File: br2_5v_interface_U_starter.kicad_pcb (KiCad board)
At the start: 4 copper layers, 94 x 76.2 mm, 18 parts, among them J10 BR2_BANK_A_J10, J11 BR2_BANK_B_J11, J12 BR2_BANK_B_J12, J13 BR2_BANK_B_J13, J14 BR2_BANK_B_J14, J17 BR2_CONTROL_J17, J18 BR2_CONTROL_J18, J19 BR2_CONTROL_J19, J20 BR2_CONTROL_J20, J21 5V_OUTPUTS_U1, J7 BR2_BANK_A_J7, J8 BR2_BANK_A_J8, J9 BR2_BANK_A_J9, U1 SN74AHCT245N

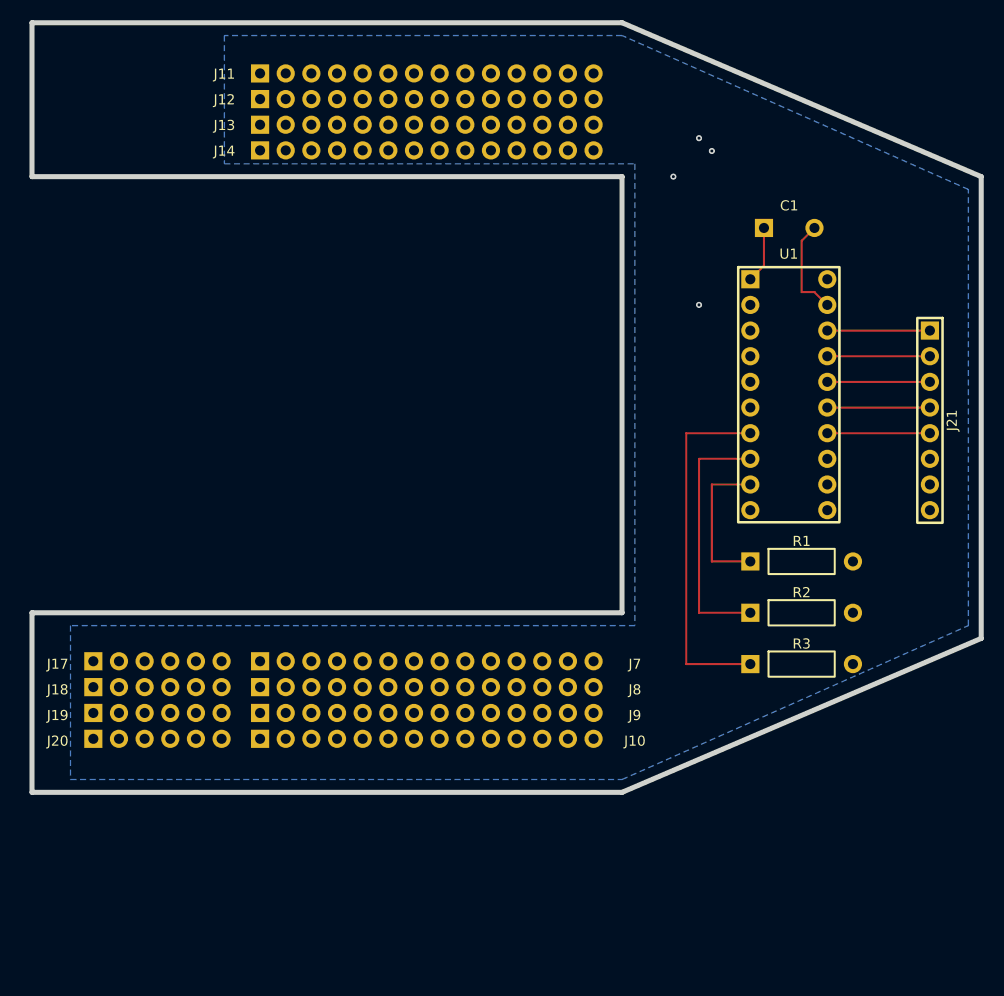
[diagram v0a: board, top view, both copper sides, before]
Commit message: Mac version: align BR2 headers and update PCB routing
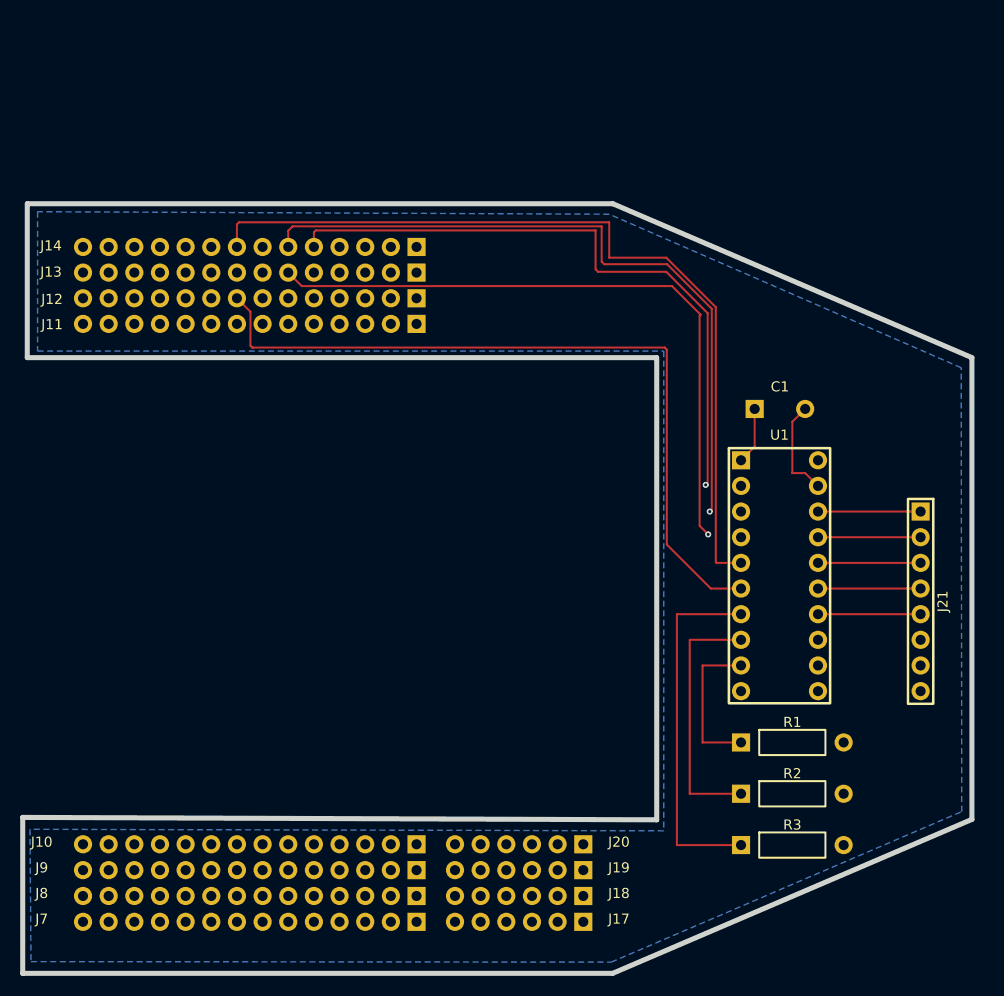
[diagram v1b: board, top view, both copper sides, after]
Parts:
- moved J17 54.9 mm to (148.6, 137.3), turned to 180 degrees
- moved J18 52.7 mm to (148.6, 134.7), turned to 180 degrees
- moved J19 50.9 mm to (148.6, 132.2), turned to 180 degrees
- moved J20 49.6 mm to (148.6, 129.6), turned to 180 degrees
- moved J7 30.1 mm to (132.1, 137.3), turned to 180 degrees
- moved J11 29.2 mm to (132.1, 78.1), turned to 180 degrees
- moved J8 25.8 mm to (132.1, 134.7), turned to 180 degrees
- moved J12 25.1 mm to (132.1, 75.5), turned to 180 degrees
- moved J9 22.0 mm to (132.1, 132.2), turned to 180 degrees
- moved J13 21.3 mm to (132.1, 73.0), turned to 180 degrees
- moved J10 18.7 mm to (132.1, 129.6), turned to 180 degrees
- moved J14 18.2 mm to (132.1, 70.5), turned to 180 degrees
- moved C1 17.9 mm to (165.5, 86.5)
- moved J21 17.9 mm to (182.0, 96.7)
- moved R1 17.9 mm to (164.2, 119.5)
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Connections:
- J20 pad 1: (no net) -> +5V
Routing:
- net +5V: track 13.3 -> 65.9 mm
- net B42_ROM_CS_N: track 57.0 -> 83.0 mm
- net B30_ACIA_CS_N: track 50.2 -> 72.5 mm
- net B41_HEARTBEAT_1KHZ: track 60.5 -> 75.4 mm, vias 1 -> 0
- net B24_RAM_CS_N: track 52.2 -> 67.0 mm, vias 0 -> 1
- net B28_UART_B_CS_N: track 57.2 -> 68.3 mm, vias 2 -> 1
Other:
- outline, holes or cut-outs redrawn

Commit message: Finalize Mac PCB for fabrication
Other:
- board text added: "6502 CS/"
- board text added: "BR2 5V INTERFACE REV 1.0 © 2026 Stanley Benoit"
- board text added: "FPGA CTRL Port"
- board text added: "FPGA Port A"
- board text added: "FPGA Port B"

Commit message: Correct 5V and 3.3V connections
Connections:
- J20 pad 1: +5V -> +3.3vdc
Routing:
- net +5V: track 65.9 -> 66.9 mm

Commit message: Update BR2 interface PCB and schematic with corrected pin mappings
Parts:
- C1: value 0.1uF -> 0.1uf
- J9: value BR2_BANK_A_J9 -> BR2_BANK _A_J9
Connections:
- net ACIA_CS_N_5V renamed /ACIA_CS_N_5V
- net B41_HEARTBEAT_1KHZ renamed /B41_HEARTBEAT_1KHZ
- net HEARTBEAT_1KHZ_5V renamed /HEARTBEAT_1KHZ_5V
- net RAM_CS_N_5V renamed /RAM_CS_N_5V
- net ROM_CS_N_5V renamed /ROM_CS_N_5V
- net UART_B_CS_N_5V renamed /UART_B_CS_N_5V
- J10 pad 1: (no net) -> unconnected-(J10-Pin_1-Pad1)
- J10 pad 10: (no net) -> unconnected-(J10-Pin_10-Pad10)
- J10 pad 11: (no net) -> unconnected-(J10-Pin_11-Pad11)
- J10 pad 12: (no net) -> unconnected-(J10-Pin_12-Pad12)
- J10 pad 13: (no net) -> unconnected-(J10-Pin_13-Pad13)
- J10 pad 14: (no net) -> unconnected-(J10-Pin_14-Pad14)
- J10 pad 2: (no net) -> unconnected-(J10-Pin_2-Pad2)
- J10 pad 3: (no net) -> unconnected-(J10-Pin_3-Pad3)
- J10 pad 4: (no net) -> unconnected-(J10-Pin_4-Pad4)
- J10 pad 5: (no net) -> unconnected-(J10-Pin_5-Pad5)
- J10 pad 6: (no net) -> unconnected-(J10-Pin_6-Pad6)
- J10 pad 7: (no net) -> unconnected-(J10-Pin_7-Pad7)
- J10 pad 8: (no net) -> unconnected-(J10-Pin_8-Pad8)
- J10 pad 9: (no net) -> unconnected-(J10-Pin_9-Pad9)
- J11 pad 10: (no net) -> unconnected-(J11-Pin_10-Pad10)
- J11 pad 11: (no net) -> unconnected-(J11-Pin_11-Pad11)
- J11 pad 12: (no net) -> unconnected-(J11-Pin_12-Pad12)
- J11 pad 13: (no net) -> unconnected-(J11-Pin_13-Pad13)
- J11 pad 14: (no net) -> unconnected-(J11-Pin_14-Pad14)
- J11 pad 2: (no net) -> unconnected-(J11-Pin_2-Pad2)
- J11 pad 3: (no net) -> unconnected-(J11-Pin_3-Pad3)
- J11 pad 4: (no net) -> unconnected-(J11-Pin_4-Pad4)
- J11 pad 5: (no net) -> /B24_RAM_CS_N
- J11 pad 6: (no net) -> /B30_ACIA_CS_N
- J11 pad 7: (no net) -> unconnected-(J11-Pin_7-Pad7)
- J11 pad 8: (no net) -> /B42_ROM_CS_N
- J11 pad 9: (no net) -> unconnected-(J11-Pin_9-Pad9)
- J12 pad 1: GND -> unconnected-(J12-Pin_1-Pad1)
- J12 pad 10: (no net) -> unconnected-(J12-Pin_10-Pad10)
- J12 pad 11: (no net) -> unconnected-(J12-Pin_11-Pad11)
- J12 pad 12: (no net) -> unconnected-(J12-Pin_12-Pad12)
- J12 pad 13: (no net) -> unconnected-(J12-Pin_13-Pad13)
- J12 pad 14: (no net) -> unconnected-(J12-Pin_14-Pad14)
- J12 pad 2: (no net) -> unconnected-(J12-Pin_2-Pad2)
- J12 pad 3: (no net) -> unconnected-(J12-Pin_3-Pad3)
- J12 pad 4: (no net) -> unconnected-(J12-Pin_4-Pad4)
- J12 pad 5: (no net) -> /B28_UART_B_CS_N
- J12 pad 6: (no net) -> unconnected-(J12-Pin_6-Pad6)
- J12 pad 7: (no net) -> unconnected-(J12-Pin_7-Pad7)
- J12 pad 9: (no net) -> unconnected-(J12-Pin_9-Pad9)
- J13 pad 1: GND -> unconnected-(J13-Pin_1-Pad1)
- J13 pad 10: (no net) -> unconnected-(J13-Pin_10-Pad10)
- J13 pad 11: (no net) -> unconnected-(J13-Pin_11-Pad11)
- J13 pad 12: (no net) -> unconnected-(J13-Pin_12-Pad12)
- J13 pad 13: (no net) -> unconnected-(J13-Pin_13-Pad13)
- J13 pad 14: (no net) -> unconnected-(J13-Pin_14-Pad14)
- J13 pad 2: (no net) -> unconnected-(J13-Pin_2-Pad2)
- J13 pad 3: (no net) -> unconnected-(J13-Pin_3-Pad3)
- J13 pad 4: (no net) -> unconnected-(J13-Pin_4-Pad4)
- J13 pad 5: (no net) -> unconnected-(J13-Pin_5-Pad5)
- J13 pad 6: B28_UART_B_CS_N -> unconnected-(J13-Pin_6-Pad6)
- J13 pad 7: (no net) -> unconnected-(J13-Pin_7-Pad7)
- J13 pad 8: (no net) -> unconnected-(J13-Pin_8-Pad8)
- J13 pad 9: (no net) -> unconnected-(J13-Pin_9-Pad9)
- J14 pad 1: GND -> unconnected-(J14-Pin_1-Pad1)
- J14 pad 10: (no net) -> unconnected-(J14-Pin_10-Pad10)
- J14 pad 11: (no net) -> unconnected-(J14-Pin_11-Pad11)
- J14 pad 12: (no net) -> unconnected-(J14-Pin_12-Pad12)
- J14 pad 13: (no net) -> unconnected-(J14-Pin_13-Pad13)
- J14 pad 14: (no net) -> unconnected-(J14-Pin_14-Pad14)
- J14 pad 2: (no net) -> unconnected-(J14-Pin_2-Pad2)
- J14 pad 3: (no net) -> unconnected-(J14-Pin_3-Pad3)
- J14 pad 4: (no net) -> unconnected-(J14-Pin_4-Pad4)
- J14 pad 5: B24_RAM_CS_N -> unconnected-(J14-Pin_5-Pad5)
- J14 pad 6: B30_ACIA_CS_N -> unconnected-(J14-Pin_6-Pad6)
- J14 pad 7: (no net) -> unconnected-(J14-Pin_7-Pad7)
- J14 pad 8: B42_ROM_CS_N -> unconnected-(J14-Pin_8-Pad8)
- J14 pad 9: (no net) -> unconnected-(J14-Pin_9-Pad9)
- J17 pad 1: (no net) -> unconnected-(J17-Pin_1-Pad1)
- J17 pad 2: (no net) -> unconnected-(J17-Pin_2-Pad2)
- J17 pad 3: (no net) -> unconnected-(J17-Pin_3-Pad3)
- J17 pad 4: (no net) -> unconnected-(J17-Pin_4-Pad4)
- J17 pad 5: (no net) -> unconnected-(J17-Pin_5-Pad5)
- J17 pad 6: (no net) -> unconnected-(J17-Pin_6-Pad6)
- J18 pad 1: (no net) -> unconnected-(J18-Pin_1-Pad1)
- J18 pad 2: (no net) -> unconnected-(J18-Pin_2-Pad2)
- J18 pad 3: (no net) -> unconnected-(J18-Pin_3-Pad3)
- J18 pad 4: (no net) -> unconnected-(J18-Pin_4-Pad4)
- J18 pad 5: (no net) -> unconnected-(J18-Pin_5-Pad5)
- J18 pad 6: (no net) -> unconnected-(J18-Pin_6-Pad6)
- J19 pad 2: (no net) -> unconnected-(J19-Pin_2-Pad2)
- J19 pad 3: (no net) -> unconnected-(J19-Pin_3-Pad3)
- J19 pad 4: (no net) -> unconnected-(J19-Pin_4-Pad4)
- J19 pad 5: (no net) -> unconnected-(J19-Pin_5-Pad5)
- J19 pad 6: (no net) -> unconnected-(J19-Pin_6-Pad6)
- J20 pad 2: (no net) -> unconnected-(J20-Pin_2-Pad2)
- J20 pad 3: (no net) -> unconnected-(J20-Pin_3-Pad3)
- J20 pad 4: (no net) -> unconnected-(J20-Pin_4-Pad4)
- J20 pad 5: (no net) -> unconnected-(J20-Pin_5-Pad5)
- J20 pad 6: (no net) -> unconnected-(J20-Pin_6-Pad6)
- J21 pad 6: (no net) -> unconnected-(J21-Pin_6-Pad6)
- J21 pad 7: (no net) -> unconnected-(J21-Pin_7-Pad7)
- J21 pad 8: (no net) -> unconnected-(J21-Pin_8-Pad8)
- J7 pad 1: (no net) -> unconnected-(J7-Pin_1-Pad1)
- J7 pad 10: (no net) -> unconnected-(J7-Pin_10-Pad10)
- J7 pad 11: (no net) -> unconnected-(J7-Pin_11-Pad11)
- J7 pad 12: (no net) -> unconnected-(J7-Pin_12-Pad12)
- J7 pad 13: (no net) -> unconnected-(J7-Pin_13-Pad13)
- J7 pad 14: (no net) -> unconnected-(J7-Pin_14-Pad14)
- J7 pad 2: (no net) -> unconnected-(J7-Pin_2-Pad2)
- J7 pad 3: (no net) -> unconnected-(J7-Pin_3-Pad3)
- J7 pad 4: (no net) -> unconnected-(J7-Pin_4-Pad4)
- J7 pad 5: (no net) -> unconnected-(J7-Pin_5-Pad5)
- J7 pad 6: (no net) -> unconnected-(J7-Pin_6-Pad6)
- J7 pad 7: (no net) -> unconnected-(J7-Pin_7-Pad7)
- J7 pad 8: (no net) -> unconnected-(J7-Pin_8-Pad8)
- J7 pad 9: (no net) -> unconnected-(J7-Pin_9-Pad9)
- J8 pad 1: (no net) -> unconnected-(J8-Pin_1-Pad1)
- J8 pad 10: (no net) -> unconnected-(J8-Pin_10-Pad10)
- J8 pad 11: (no net) -> unconnected-(J8-Pin_11-Pad11)
- J8 pad 12: (no net) -> unconnected-(J8-Pin_12-Pad12)
- J8 pad 13: (no net) -> unconnected-(J8-Pin_13-Pad13)
- J8 pad 14: (no net) -> unconnected-(J8-Pin_14-Pad14)
- J8 pad 2: (no net) -> unconnected-(J8-Pin_2-Pad2)
- J8 pad 3: (no net) -> unconnected-(J8-Pin_3-Pad3)
- J8 pad 4: (no net) -> unconnected-(J8-Pin_4-Pad4)
- J8 pad 5: (no net) -> unconnected-(J8-Pin_5-Pad5)
- J8 pad 6: (no net) -> unconnected-(J8-Pin_6-Pad6)
- J8 pad 7: (no net) -> unconnected-(J8-Pin_7-Pad7)
- J8 pad 8: (no net) -> unconnected-(J8-Pin_8-Pad8)
- J8 pad 9: (no net) -> unconnected-(J8-Pin_9-Pad9)
- J9 pad 1: (no net) -> unconnected-(J9-Pin_1-Pad1)
- J9 pad 10: (no net) -> unconnected-(J9-Pin_10-Pad10)
- J9 pad 11: (no net) -> unconnected-(J9-Pin_11-Pad11)
- J9 pad 12: (no net) -> unconnected-(J9-Pin_12-Pad12)
- J9 pad 13: (no net) -> unconnected-(J9-Pin_13-Pad13)
- J9 pad 14: (no net) -> unconnected-(J9-Pin_14-Pad14)
- J9 pad 2: (no net) -> unconnected-(J9-Pin_2-Pad2)
- J9 pad 3: (no net) -> unconnected-(J9-Pin_3-Pad3)
- J9 pad 4: (no net) -> unconnected-(J9-Pin_4-Pad4)
- J9 pad 5: (no net) -> unconnected-(J9-Pin_5-Pad5)
- J9 pad 6: (no net) -> unconnected-(J9-Pin_6-Pad6)
- J9 pad 7: (no net) -> unconnected-(J9-Pin_7-Pad7)
- J9 pad 8: (no net) -> unconnected-(J9-Pin_8-Pad8)
- J9 pad 9: (no net) -> unconnected-(J9-Pin_9-Pad9)
- R1 pad 1: A7_PULLDOWN -> GND
- R1 pad 2: GND -> Net-(U1-A7)
- R2 pad 1: A6_PULLDOWN -> GND
- R2 pad 2: GND -> Net-(U1-A6)
- R3 pad 1: A5_PULLDOWN -> GND
- R3 pad 2: GND -> Net-(U1-A5)
- U1 pad 11: (no net) -> unconnected-(U1-B7-Pad11)
- U1 pad 12: (no net) -> unconnected-(U1-B6-Pad12)
- U1 pad 13: (no net) -> unconnected-(U1-B5-Pad13)
- U1 pad 2: B24_RAM_CS_N -> /B24_RAM_CS_N
- U1 pad 3: B30_ACIA_CS_N -> /B30_ACIA_CS_N
- U1 pad 4: B28_UART_B_CS_N -> /B28_UART_B_CS_N
- U1 pad 5: B42_ROM_CS_N -> /B42_ROM_CS_N
- U1 pad 7: A5_PULLDOWN -> Net-(U1-A5)
- U1 pad 8: A6_PULLDOWN -> Net-(U1-A6)
- U1 pad 9: A7_PULLDOWN -> Net-(U1-A7)
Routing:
- net B42_ROM_CS_N: track 83.0 -> 0.00 mm
- net B30_ACIA_CS_N: track 72.5 -> 0.00 mm, vias 1 -> 0
- net /B42_ROM_CS_N: track 0.00 -> 72.4 mm
- net B28_UART_B_CS_N: track 68.3 -> 0.00 mm, vias 1 -> 0
- net B24_RAM_CS_N: track 67.0 -> 0.00 mm, vias 1 -> 0
- net /B30_ACIA_CS_N: track 0.00 -> 62.1 mm
- net /B28_UART_B_CS_N: track 0.00 -> 61.3 mm, vias 0 -> 1
- net /B24_RAM_CS_N: track 0.00 -> 56.3 mm
- net A5_PULLDOWN: track 35.6 -> 0.00 mm
- net Net-(U1-A5): track 0.00 -> 28.6 mm
- net A6_PULLDOWN: track 25.4 -> 0.00 mm
- net Net-(U1-A6): track 0.00 -> 21.6 mm
- net GND: track 9.94 -> 25.2 mm
- net A7_PULLDOWN: track 15.2 -> 0.00 mm
- net Net-(U1-A7): track 0.00 -> 13.3 mm
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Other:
- board text added: "BR2 5V INTERFACE REV 1.1 © 2026 Stanley Benoit"
- board text added: "J11 BR2"
- board text added: "J12 BR2"
- board text added: "J13 BR2"
- board text added: "J14 BR2"
- board text removed: "BR2 5V INTERFACE REV 1.0 © 2026 Stanley Benoit"
